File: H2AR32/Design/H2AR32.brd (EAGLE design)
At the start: 34.6 x 30 mm, 57 parts, among them P1 HEXABIT__NO_P1_P5_P6_P7_P12, U1 STM32G0B1CEU6N, U2 INA199B2DCKT, U3 INA199B1DCKT, U4 TEXAS_INSTRUMENTS_REF2033AIDD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, X1 XTALL_CSTCE8M00G52

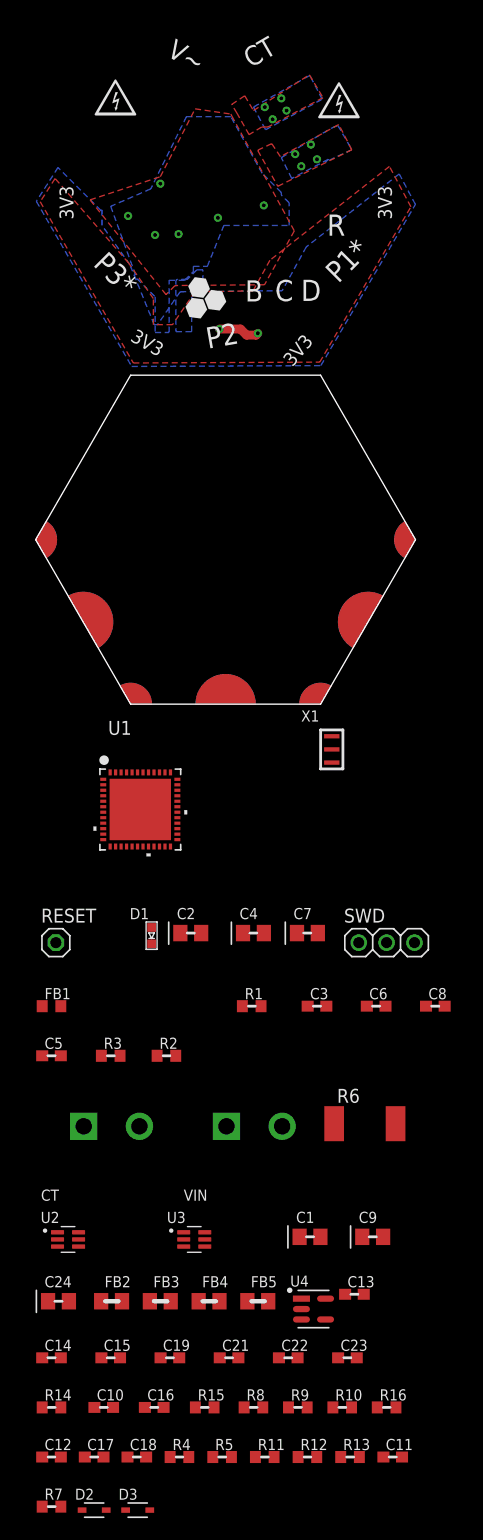
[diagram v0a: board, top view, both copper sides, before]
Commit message: -Update the pcb layout design to be based on 4 layers for better performance and improve the analog design
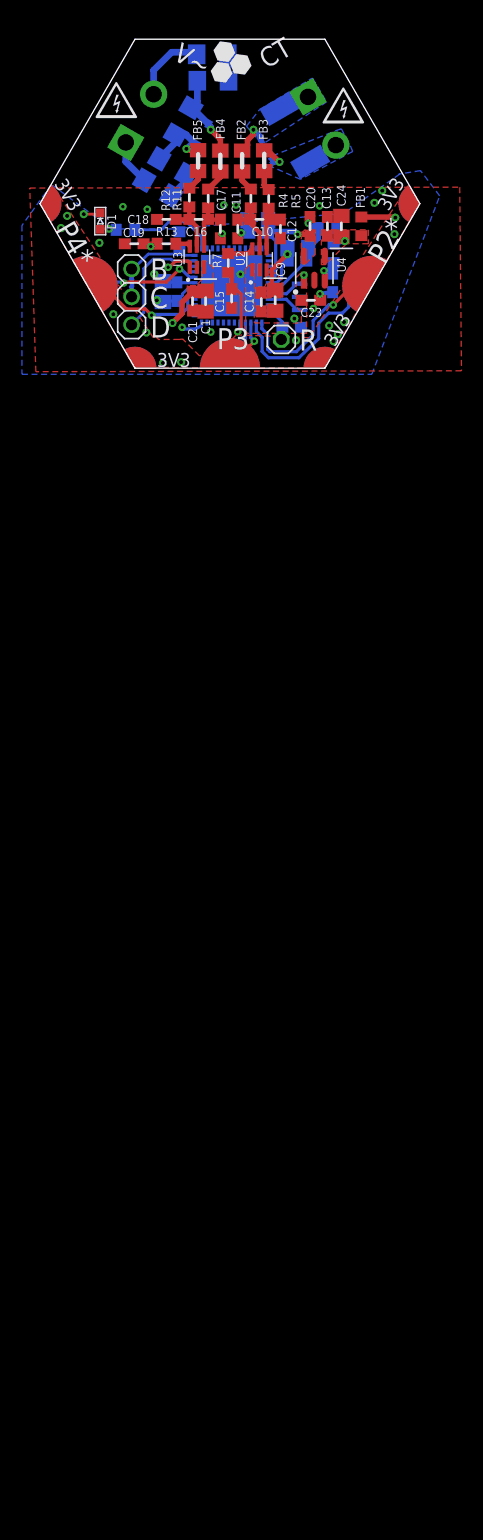
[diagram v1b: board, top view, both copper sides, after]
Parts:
- added C20: 100nF, HEXABITZ_RCLS:C-0603
- R10, R14, R16, R8, R9: device HEXABITZ_RCLS:R-0603 -> HEXABITZ_RCLS:R1206
- moved D3 125.6 mm to (-2.18, 21.2), flipped to the bottom, turned to 120 degrees
- moved D2 125.0 mm to (3.68, 19.8), flipped to the bottom, turned to 60 degrees
- moved R8 123.5 mm to (-1.29, 28.5), flipped to the bottom
- moved R10 121.6 mm to (-1.23, 26.1), flipped to the bottom, turned to 180 degrees
- moved R14 117.9 mm to (-3.95, 22.4), flipped to the bottom, turned to 120 degrees
- moved R12 115.4 mm to (-3.38, 15.5), turned to 270 degrees
- moved R4 115.0 mm to (2.22, 15.4), turned to 270 degrees
- moved R11 114.9 mm to (-1.67, 15.4), turned to 270 degrees
- moved R5 114.8 mm to (3.85, 15.4), turned to 270 degrees
- moved R7 114.6 mm to (0.16, 9.53), turned to 270 degrees
- moved C12 113.9 mm to (4.92, 12.6), turned to 270 degrees
- moved R9 113.7 mm to (-4.90, 18.3), flipped to the bottom, turned to 210 degrees
- moved R16 113.1 mm to (-6.27, 16.4), flipped to the bottom, turned to 30 degrees
- moved C18 112.9 mm to (-5.48, 13.5), turned to 180 degrees
- moved C11 112.9 mm to (1.03, 12.6), turned to 90 degrees
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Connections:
- net V_REF renamed VBAIS
- removed net AGND: C1.2, C11.1, C12.2, C13.2, C14.2, C15.2, C17.1, C18.2, C19.2, C2.2, C21.2, C22.2, C23.2, C24.2, C5.2, C7.2, C8.2, C9.2, R2.2, U1.7, U2.2, U3.2, U4.2
- removed net N$28: R1.2, U1.25
- removed net USART5_RX: P1.PAD_PD3, U1.43
- removed net USART5_TX: P1.PAD_PU3, U1.42
- removed net VCC: C1.1, C13.1, C14.1, C2.1, C21.1, C24.1, C5.1, C7.1, C8.1, C9.1, FB1.1, R15.2, U1.4, U1.5, U1.6, U2.3, U3.3, U4.4
- new net N$1: R1.2, U1.37
- new net USART6_RX: P1.PAD_PD3, U1.16
- new net USART6_TX: P1.PAD_PU3, U1.15
- new net VBAT: U1.4
- new net VDDA: C1.1, C13.1, C14.1, C21.1, C24.1, C7.1, C8.1, C9.1, FB1.1, R15.2, U1.6, U2.3, U3.3, U4.4
- new net VSSA: C1.2, C11.1, C12.2, C13.2, C14.2, C15.2, C17.1, C18.2, C19.2, C2.2, C20.2, C21.2, C22.2, C23.2, C24.2, C5.2, C7.2, C8.2, C9.2, R2.2, U1.7, U2.2, U3.2, U4.2
- net CURRENT_SENSE: now also U1.17; no longer U1.24
- net GND: no longer U1.48
- net USART1*_RX: now also P1.PAD_PD4; no longer P1.PAD_PD2
- net USART1*_TX: now also P1.PAD_PU4; no longer P1.PAD_PU2
- net USART2*_RX: now also P1.PAD_PD2; no longer P1.PAD_PD4
- net USART2*_TX: now also P1.PAD_PU2; no longer P1.PAD_PU4
- net VOLTAGE_SENSE: now also U1.24; no longer U1.16
- net VREF: now also C2.1, C20.1, C5.1, U1.5
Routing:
- net VDDA: track 0.00 -> 37.8 mm, vias 0 -> 3
- net USART2*_RX: track 0.00 -> 16.6 mm
- net VBAIS: track 0.00 -> 15.8 mm, vias 0 -> 2
- net USART2*_TX: track 0.00 -> 15.1 mm, vias 0 -> 1
- net VOLTAGE_SENSE: track 0.00 -> 14.2 mm, vias 0 -> 2
- net VSSA: track 0.00 -> 12.8 mm, vias 0 -> 11
- net USART1*_TX: track 0.00 -> 11.9 mm, vias 0 -> 1
- net DATA: track 0.00 -> 10.6 mm
- net USART1*_RX: track 0.00 -> 10.0 mm, vias 0 -> 2
- net VREF: track 0.00 -> 9.97 mm, vias 0 -> 1
- net CLK: track 0.00 -> 9.21 mm
- net N$1: track 0.00 -> 7.99 mm
- net N$21: track 0.00 -> 7.78 mm, vias 0 -> 1
- net N$22: track 0.00 -> 7.31 mm, vias 0 -> 1
- net CURRENT_SENSE: track 0.00 -> 7.20 mm, vias 0 -> 1
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- added copper zone on layer 16, net CT_3
- added copper zone on layer 16, net CT_4
- added copper zone on layer 2, net GND
- added copper zone on layer 1, net VBAIS
- added copper zone on layer 15, net VDD
- added copper zone on layer 1, net VDDA
- added copper zone on layer 1, net VREF
- added copper zone on layer 1, net VSSA
- added copper zone on layer 2, net VSSA
- removed copper zone on layer 1, net AGND
- removed copper zone on layer 16, net AGND
- removed copper zone on layer 1, net CT_1
- removed copper zone on layer 16, net CT_1
- removed copper zone on layer 1, net CT_2
- removed copper zone on layer 16, net CT_2
- removed copper zone on layer 16, net VCC
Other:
- board text added: "P2*"
- board text added: "P3"
- board text added: "P4*"
- board text removed: "P1*"
- board text removed: "P2"
- board text removed: "P3*"
